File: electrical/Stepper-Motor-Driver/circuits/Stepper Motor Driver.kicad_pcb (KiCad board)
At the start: 4 copper layers, 155 parts, among them J1 Screw_Terminal_01x03, J2 Screw_Terminal_01x04, Q1 IRF530NPBF, Q2 IRF530NPBF, Q3 IRF530NPBF, Q4 IRF530NPBF, Q5 IRF530NPBF, Q6 IRF530NPBF, Q7 IRF530NPBF, Q8 IRF530NPBF, U10 LM1117-Q1, U11 TPS54202DDC, U12 REF2033, U2 UCC27710D, U3 UCC27710D, U4 UCC27710D, U5 UCC27710D, U6 INA240A2PW, U7 ADS7042xDCU, U8 INA240A2PW, U9 ADS7042xDCU

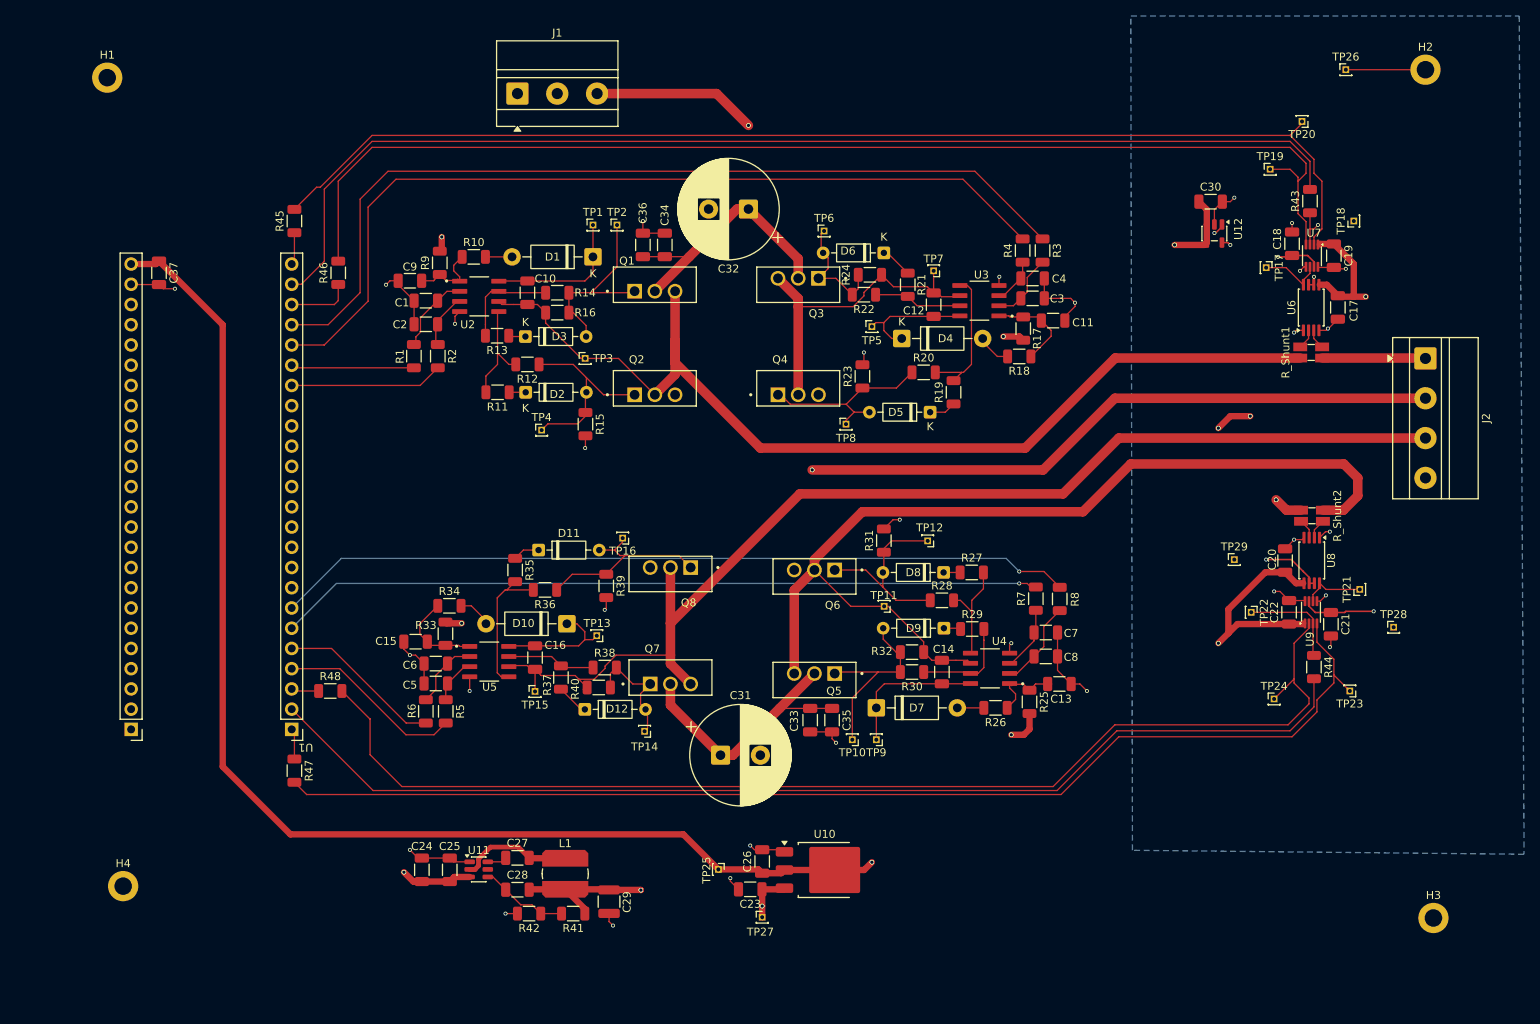
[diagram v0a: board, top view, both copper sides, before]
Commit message: Ensuring continuous ground plane below analog section
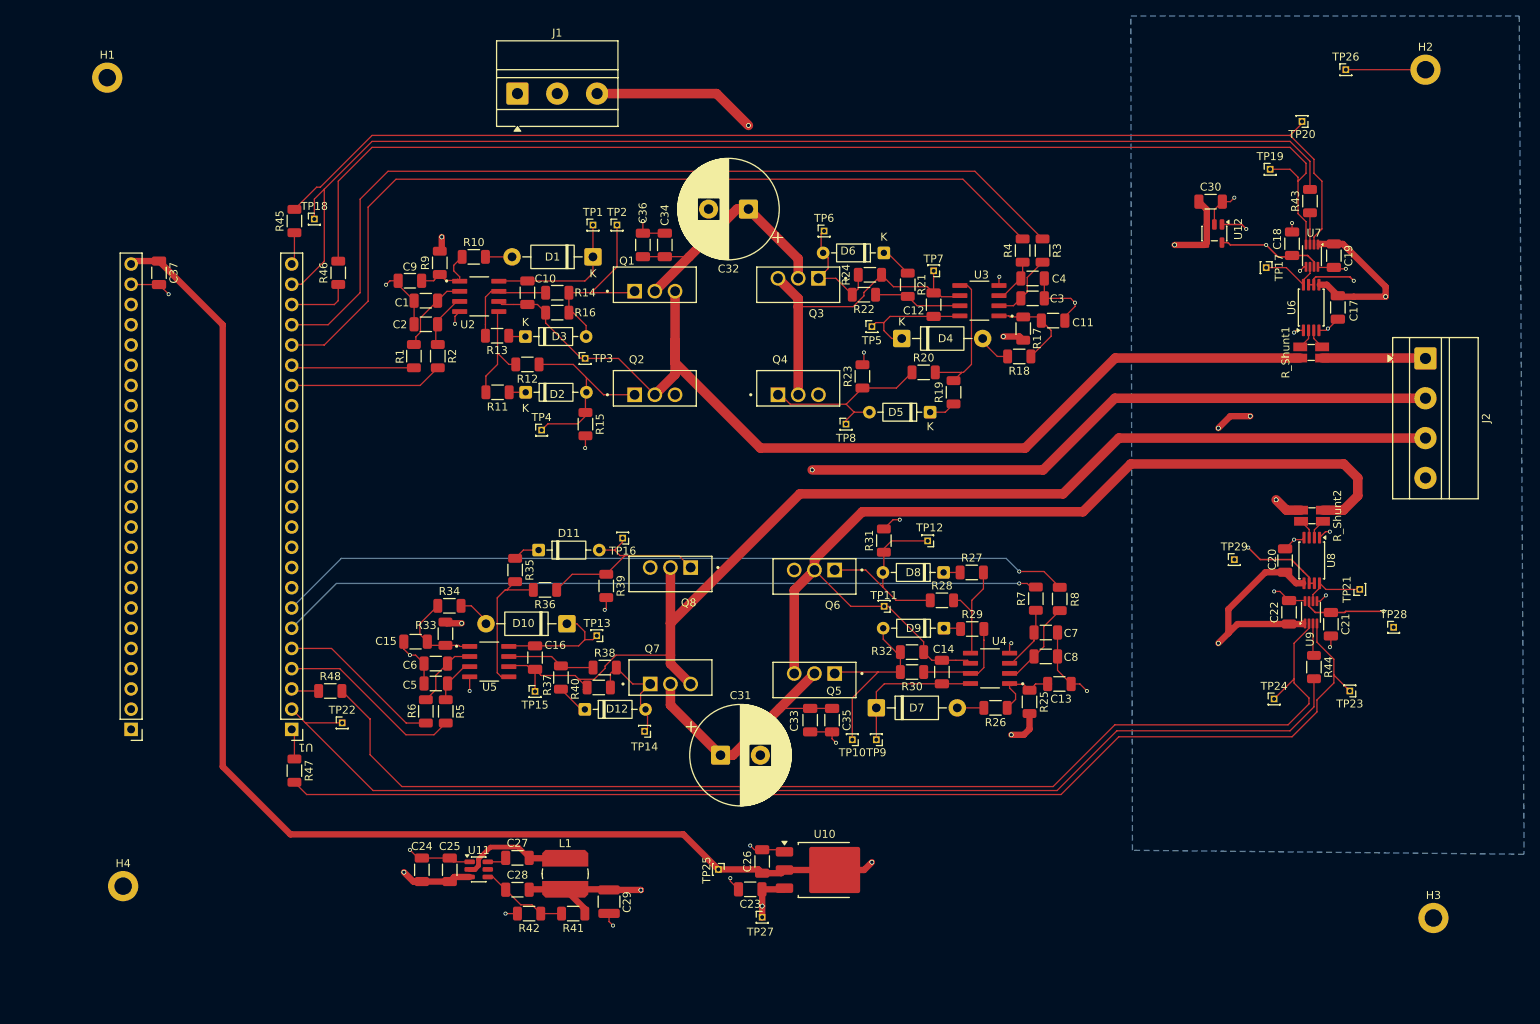
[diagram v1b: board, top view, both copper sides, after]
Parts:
- moved TP18 130.5 mm to (138.5, 34.2), turned to 0 degrees
- moved TP22 115.0 mm to (142.0, 97.5), turned to 0 degrees
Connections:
- TP18 pad 1: /Current Sensor A/SDO -> /SDOA
- TP22 pad 1: /Current Sensor B/SDO -> /SDOB
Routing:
- net +1.65V-REF: track 68.6 -> 89.7 mm
- net /Current Sensor B/SDO: track 12.1 -> 4.07 mm
- net /Current Sensor A/SDO: track 9.90 -> 3.99 mm, vias 1 -> 0
- net /SDOB: track 140.8 -> 145.5 mm
- net /SDOA: track 145.1 -> 149.4 mm
- net +3.3V: track 316.4 -> 320.2 mm
- net GND: track 120.0 -> 119.5 mm
- net +3.3V-REF: vias 3 -> 2

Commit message: Moved power section
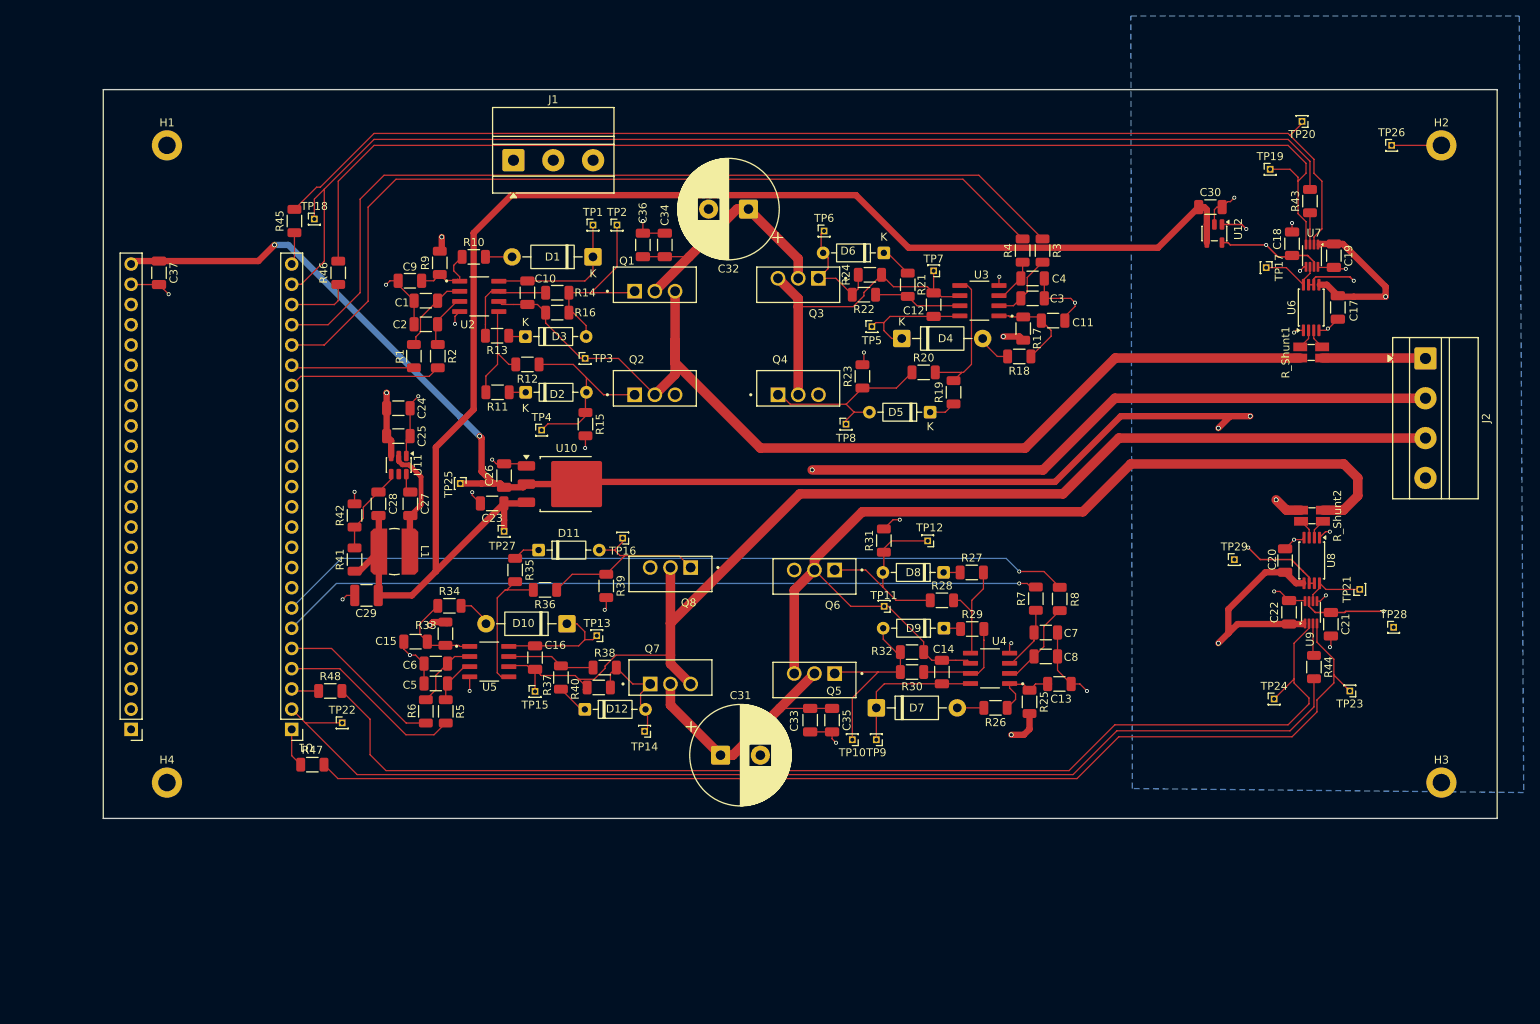
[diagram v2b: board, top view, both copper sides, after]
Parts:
- moved C23 58.3 mm to (160.8, 70.0)
- moved C26 58.3 mm to (162.3, 66.5)
- moved TP25 58.3 mm to (156.8, 67.5)
- moved TP27 58.3 mm to (162.3, 73.5)
- moved U10 58.3 mm to (170.2, 67.5)
- moved C24 58.0 mm to (149.1, 58.0), turned to 180 degrees
- moved C25 54.8 mm to (149.1, 61.5), turned to 180 degrees
- moved R42 54.6 mm to (143.6, 71.5), turned to 90 degrees
- moved R41 52.2 mm to (143.6, 77.0), turned to 90 degrees
- moved U11 51.7 mm to (149.1, 65.1), turned to -90 degrees
- moved C28 51.5 mm to (146.6, 70.0), turned to -90 degrees
- moved C29 49.0 mm to (145.1, 81.5), turned to 0 degrees
- moved C27 46.4 mm to (150.6, 70.0), turned to -90 degrees
- moved L1 45.8 mm to (148.6, 76.0), turned to -90 degrees
- moved H3 17.0 mm to (280.0, 105.0)
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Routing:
- net +3.3V: track 320.2 -> 267.2 mm, vias 5 -> 6
- net +12V: track 258.4 -> 229.0 mm
- net +VMotor: track 168.5 -> 159.4 mm, vias 1 -> 0
- net +5V: track 179.7 -> 188.7 mm, vias 3 -> 0
- net GND: track 119.5 -> 114.3 mm
- net /~{CS}B: track 149.0 -> 144.5 mm
- net /SCLKB: track 148.5 -> 146.8 mm
- net /SDOB: track 145.5 -> 143.8 mm
- net Net-(U1-IOB31B): track 3.86 -> 5.38 mm
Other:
- board outline added: 175 x 91.5 mm

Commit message: Compressing layout to 100mm x 100mm
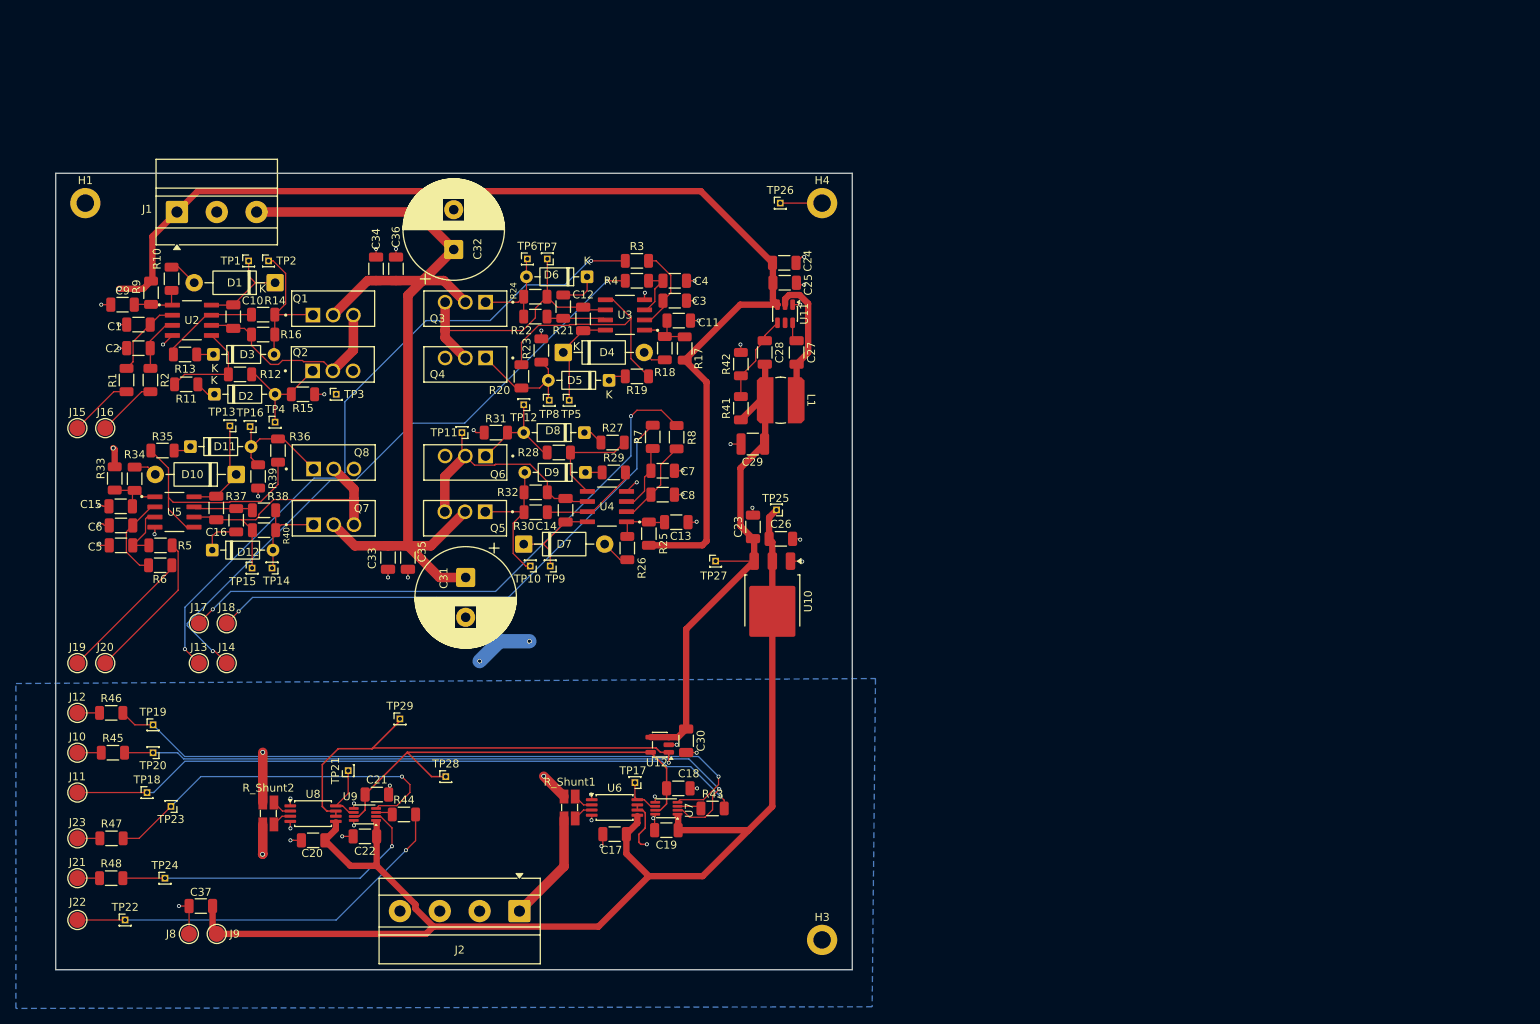
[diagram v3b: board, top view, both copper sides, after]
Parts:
- removed H2: MountingHole_Pad, MountingHole:MountingHole_2.2mm_M2_DIN965_Pad
- removed U1: ~, Tang Nano 9k:Tang Nano 9k Header Pins
- added J10: Conn_01x01_Socket, TestPoint:TestPoint_Pad_D2.0mm, F.Cu at (108.8, 101.2)
- added J11: Conn_01x01_Socket, TestPoint:TestPoint_Pad_D2.0mm, F.Cu at (108.8, 106.2)
- added J12: Conn_01x01_Socket, TestPoint:TestPoint_Pad_D2.0mm, F.Cu at (108.8, 96.2)
- added J13: Conn_01x01_Socket, TestPoint:TestPoint_Pad_D2.0mm, F.Cu at (124.0, 90.0)
- added J14: Conn_01x01_Socket, TestPoint:TestPoint_Pad_D2.0mm, F.Cu at (127.5, 90.0)
- added J15: Conn_01x01_Socket, TestPoint:TestPoint_Pad_D2.0mm, F.Cu at (108.8, 60.5)
- added J16: Conn_01x01_Socket, TestPoint:TestPoint_Pad_D2.0mm, F.Cu at (112.2, 60.5)
- added J17: Conn_01x01_Socket, TestPoint:TestPoint_Pad_D2.0mm, F.Cu at (124.0, 85.0)
- added J18: Conn_01x01_Socket, TestPoint:TestPoint_Pad_D2.0mm, F.Cu at (127.5, 85.0)
- added J19: Conn_01x01_Socket, TestPoint:TestPoint_Pad_D2.0mm, F.Cu at (108.8, 90.0)
- added J20: Conn_01x01_Socket, TestPoint:TestPoint_Pad_D2.0mm, F.Cu at (112.2, 90.0)
- added J21: Conn_01x01_Socket, TestPoint:TestPoint_Pad_D2.0mm, F.Cu at (108.8, 117.0)
- added J22: Conn_01x01_Socket, TestPoint:TestPoint_Pad_D2.0mm, F.Cu at (108.8, 122.2)
- added J23: Conn_01x01_Socket, TestPoint:TestPoint_Pad_D2.0mm, F.Cu at (108.8, 112.0)
- added J8: Conn_01x01_Socket, TestPoint:TestPoint_Pad_D2.0mm, F.Cu at (122.8, 124.0)
- added J9: Conn_01x01_Socket, TestPoint:TestPoint_Pad_D2.0mm, F.Cu at (126.2, 124.0)
- moved TP20 164.6 mm to (118.2, 101.2)
- moved TP19 156.6 mm to (118.2, 97.8)
- moved TP23 148.7 mm to (120.5, 108.0)
- moved TP24 141.1 mm to (119.8, 117.0)
- moved R_Shunt2 136.2 mm to (132.7, 108.9), turned to 0 degrees
- moved J2 133.2 mm to (164.2, 121.1), turned to 180 degrees
- moved U8 129.4 mm to (138.3, 108.9), turned to 0 degrees
- moved TP21 129.0 mm to (142.8, 103.5)
- moved C20 127.0 mm to (138.3, 112.3), turned to 0 degrees
- moved C21 121.7 mm to (146.3, 106.5), turned to 0 degrees
- moved U9 121.5 mm to (144.8, 109.0), turned to 180 degrees
- moved TP28 120.5 mm to (155.0, 104.2)
- moved C22 119.4 mm to (144.8, 111.8), turned to 180 degrees
- moved R44 115.7 mm to (149.8, 109.0), turned to 0 degrees
- moved C17 112.3 mm to (176.2, 111.5), turned to 0 degrees
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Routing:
- net +5V: track 188.7 -> 65.1 mm
- net /SCLKB: track 146.8 -> 40.4 mm, vias 0 -> 1
- net +3.3V: track 267.2 -> 164.6 mm, vias 6 -> 0
- net /~{CS}B: track 144.5 -> 45.7 mm, vias 0 -> 1
- net /SDOB: track 143.8 -> 49.9 mm, vias 0 -> 1
- net /~{CS}A: track 149.4 -> 85.2 mm, vias 0 -> 1
- net /SDOA: track 149.6 -> 85.9 mm, vias 0 -> 1
- net /SCLKA: track 147.2 -> 84.6 mm, vias 0 -> 1
- net +12V: track 229.0 -> 168.7 mm, vias 5 -> 2
- net GND: track 114.3 -> 62.6 mm, vias 31 -> 48
- net /Current Sensor B/IN+: track 121.8 -> 75.2 mm, vias 0 -> 1
- net +VMotor: track 159.4 -> 114.0 mm
- net +3.3V-REF: track 95.0 -> 56.9 mm, vias 2 -> 0
- net /H-Bridge Controller B/BR2: track 147.4 -> 114.9 mm
- net /LI2A: track 110.4 -> 80.0 mm, vias 0 -> 2
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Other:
- board size 175 x 91.5 mm -> 100 x 100 mm

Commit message: TestPoint allignment
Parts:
- moved TP23 4.59 mm to (118.2, 112.0)
- moved TP22 3.50 mm to (118.2, 122.2)
- moved TP24 1.50 mm to (118.2, 117.0)
- moved TP18 0.75 mm to (118.2, 106.2)
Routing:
- net /~{CS}B: track 45.7 -> 46.7 mm

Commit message: Adding fiducial marks
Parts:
- added C38: 33pF, Capacitor_SMD:C_1206_3216Metric, F.Cu at (192.8, 51.0)
- added FID1: Fiducial, Fiducial:Fiducial_1mm_Mask3mm, F.Cu at (109.8, 39.2)
- added FID2: Fiducial, Fiducial:Fiducial_1mm_Mask3mm, F.Cu at (202.2, 117.8)
- C28: value 68pF -> 33pF
- moved TP17 8.81 mm to (173.8, 97.8)
- moved R42 1.80 mm to (190.2, 52.5)
- moved TP28 1.75 mm to (156.8, 104.2)
- moved TP29 1.50 mm to (149.2, 95.5)
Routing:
- net Net-(U7-AINP): track 4.86 -> 14.2 mm, vias 0 -> 1
- net Net-(U11-FB): track 11.2 -> 14.0 mm
- net +5V: track 65.1 -> 67.4 mm
- net +3.3V-REF: track 56.9 -> 58.6 mm
- net +1.65V-REF: track 77.0 -> 78.5 mm
